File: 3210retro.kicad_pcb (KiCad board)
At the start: 6 copper layers, 44 x 118 mm, 188 parts, among them J801 TEST_2P, P101 USB_OTG, P103 LIPO, P104 DC, P105 EAR, P106 SPEAKER, P107 HEADPHONE, P108 RUMBLE, P301 SEPS525, P801 JTAG, Q501 MMBF170, Q701 MMBF170, SW701 SW_PUSH, SW702 C, SW703 1, SW704 4ghi, SW705 7pqrs, SW706 -, SW707 2abc, SW708 5jkl, SW709 8tuv, SW710 UP, SW711 3def, SW712 6mno, SW713 9wxyz, SW714 *+, SW715 DOWN, SW716 0space, SW717 #up, U1301 LSM9DS1, U201 MAX1555, U202 TPS62742, U203 TPS61021A, U301 TPS61041DBV, U401 LD3985G18R_TSOT23, U402 DRV8601, U403 WM8994ECS/R, U404 MP34DT01TR, U405 MP34DT01TR, U504 A7, U505 SIM_SLOT, U601 ESP-12E, U801 STM32F756VGTx, X101 ANT_GPS, X102 ANT_GSM, Y801 32kHz, Y802 24MHz

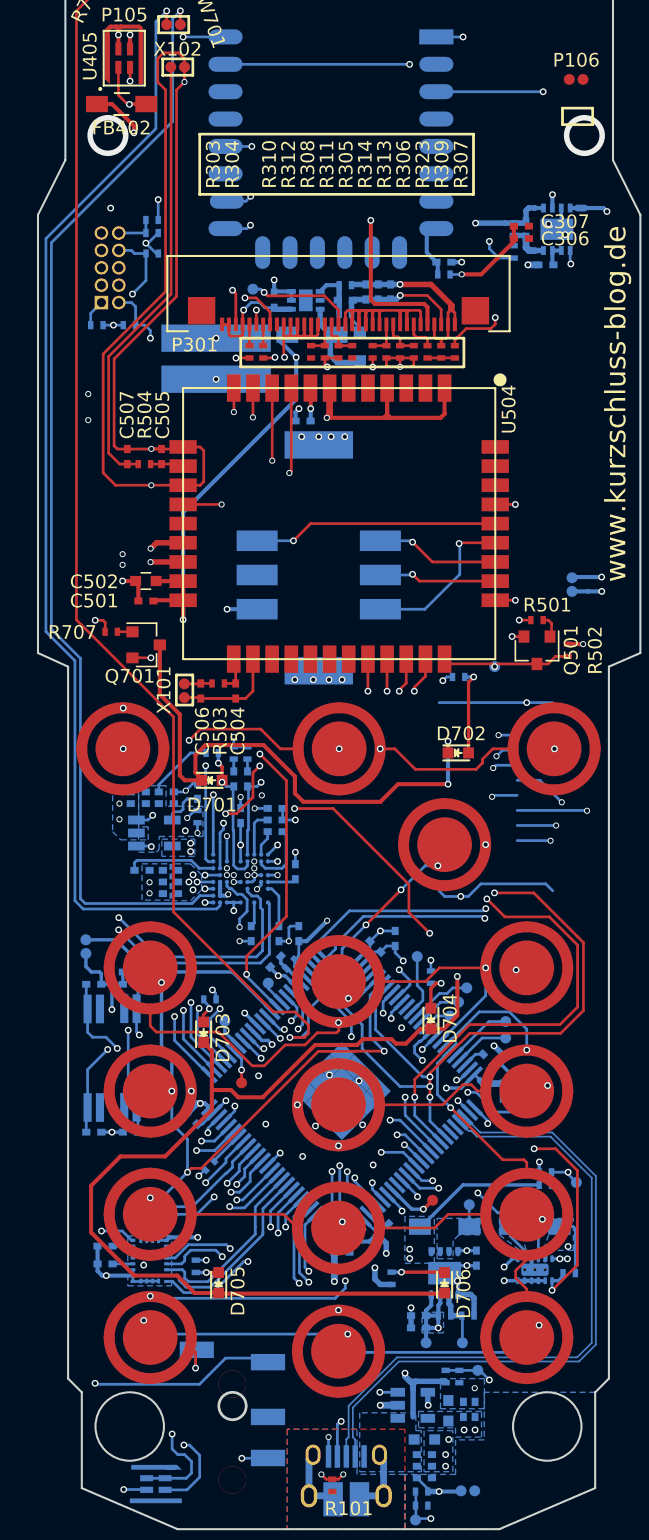
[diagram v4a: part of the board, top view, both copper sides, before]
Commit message: Board Revision 1
* Modified layout of I2C busses
* Added Micro SD footprint back in
* changed layout of crystals
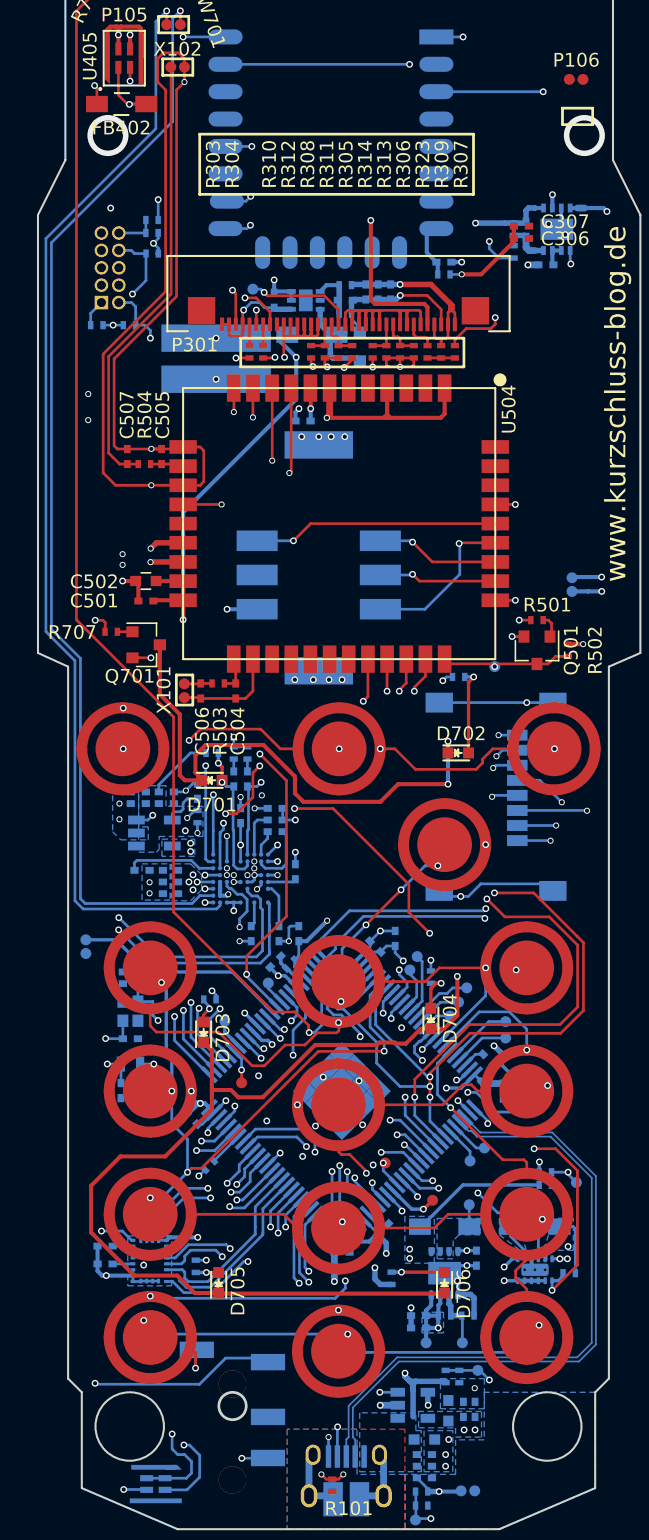
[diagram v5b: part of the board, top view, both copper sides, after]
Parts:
- added J1101: MICRO_SD_HINGE, Connectors:microSD_Card_Receptacle_Wuerth_693072010801, B.Cu at (109.7, 105.6)
- added TP111: TP, NokiaRetroFit:TP, B.Cu at (102.8, 132.3)
- added TP112: TP, NokiaRetroFit:TP, F.Cu at (104.5, 118.2)
- added TP113: TP, NokiaRetroFit:TP, F.Cu at (110.0, 131.2)
- added TP114: TP, NokiaRetroFit:TP, F.Cu at (109.0, 132.2)
- Y801: footprint Crystals:Crystal_SMD_SeikoEpson_MC146-4pin_6.7x1.5mm_HandSoldering -> Crystals:Crystal_SMD_2012-2pin_2.0x1.2mm
- Y802: footprint Crystals:Crystal_SMD_SeikoEpson_MC146-4pin_6.7x1.5mm_HandSoldering -> NokiaRetroFit:Crystal_SMD_ABM11W_4_D1X_T_-4pin_2.0x1.6mm
- moved C804 10.8 mm to (84.1, 119.2)
- moved C802 8.01 mm to (83.5, 127.1), turned to 270 degrees
- moved C801 4.54 mm to (84.8, 127.1), turned to 270 degrees
- moved C803 3.97 mm to (84.1, 123.3), turned to 0 degrees
- moved Y802 3.42 mm to (84.1, 121.3), turned to 90 degrees
- moved Y801 2.72 mm to (84.2, 125.1), turned to 180 degrees
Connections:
- R310 pad 2: /Controller/I2C3_SCL -> /Controller/I2C1_SCL
- R311 pad 2: /Controller/I2C3_SDA -> /Controller/I2C1_SDA
- R801 pad 1: NVCC_3V3 -> 3V3
- R804 pad 1: NVCC_3V3 -> 3V3
- R805 pad 1: NVCC_3V3 -> 3V3
- R807 pad 1: NVCC_3V3 -> 3V3
- U1301 pad 2: /Controller/I2C1_SCL -> /Audio Amplifier/AUDIO_I2C_SCL
- U1301 pad 4: /Controller/I2C1_SDA -> /Audio Amplifier/AUDIO_I2C_SDA
- U403 pad A2: /Audio Amplifier/SPK_OUT- -> Net-(R407-Pad2)
- U403 pad B1: /Audio Amplifier/SPK_OUT+ -> Net-(R406-Pad2)
- U505 pad 5: (no net) -> Net-(U505-Pad5)
- U801 pad 36: Net-(U801-Pad36) -> /Controller/PB2
- U801 pad 55: Net-(U801-Pad55) -> /Controller/PD8
- U801 pad 56: Net-(U801-Pad56) -> /Controller/PD9
- U801 pad 67: Net-(U801-Pad67) -> /Controller/PA8
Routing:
- net NVCC_3V3: track 237.7 -> 149.2 mm, vias 23 -> 20
- net /Audio Amplifier/AUDIO_I2C_SCL: track 43.9 -> 103.7 mm, vias 5 -> 6
- net /Controller/I2C1_SDA: track 12.1 -> 68.4 mm
- net /Controller/I2C1_SCL: track 11.8 -> 67.2 mm, vias 0 -> 2
- net /Audio Amplifier/AUDIO_I2C_SDA: track 33.6 -> 86.7 mm, vias 2 -> 3
- net 3V3: track 188.2 -> 206.1 mm, vias 8 -> 10
- net GND: track 200.2 -> 191.2 mm, vias 81 -> 79
- net Net-(C801-Pad1): track 20.2 -> 12.3 mm
- net Net-(C804-Pad1): track 21.1 -> 15.1 mm
- net /Controller/PB2: track 0.00 -> 3.32 mm
- net /Controller/PD8: track 0.00 -> 2.77 mm
- net /Controller/PD9: track 0.00 -> 2.73 mm
- net Net-(C802-Pad1): track 18.5 -> 15.8 mm
- net /Controller/SYS_WKUP: track 100.0 -> 97.4 mm
- net /Controller/PA8: track 0.00 -> 2.02 mm, vias 0 -> 1
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
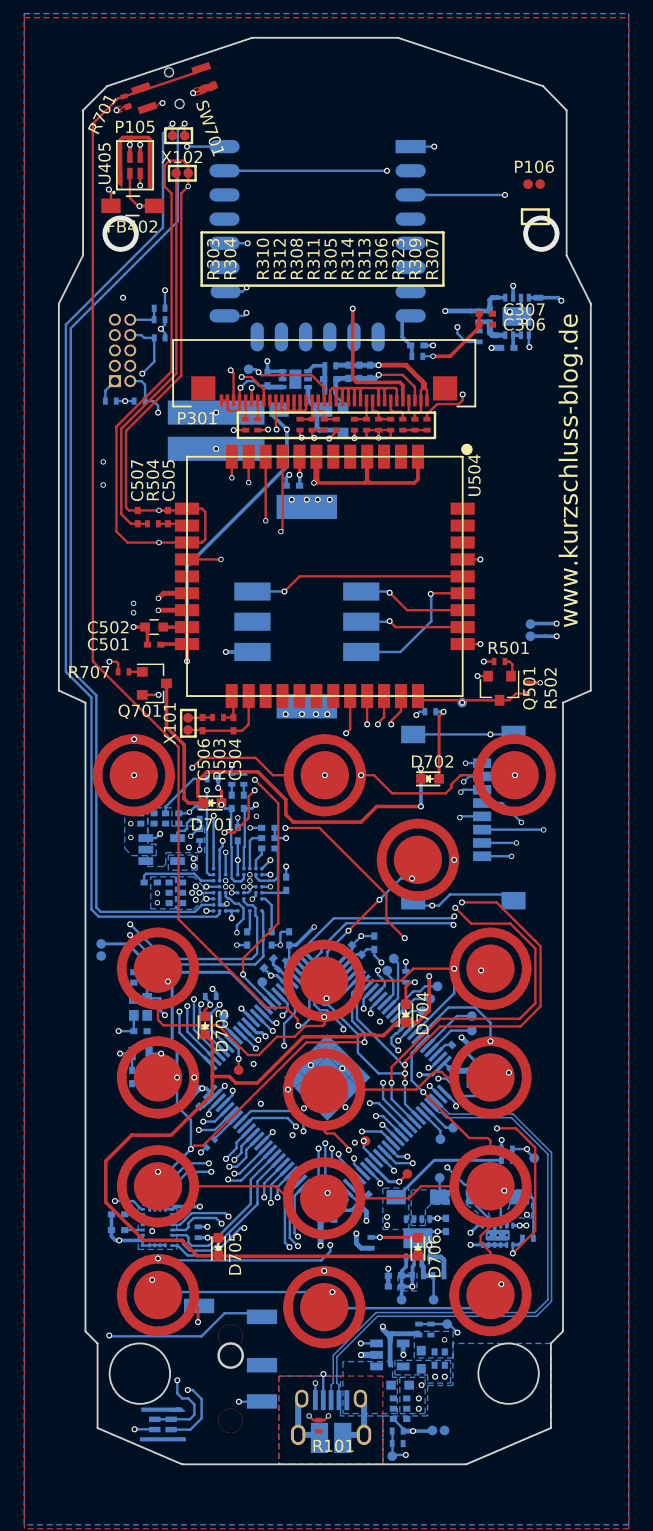
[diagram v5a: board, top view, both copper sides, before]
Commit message: changed sound subsystem
rerouted all the changed tracks
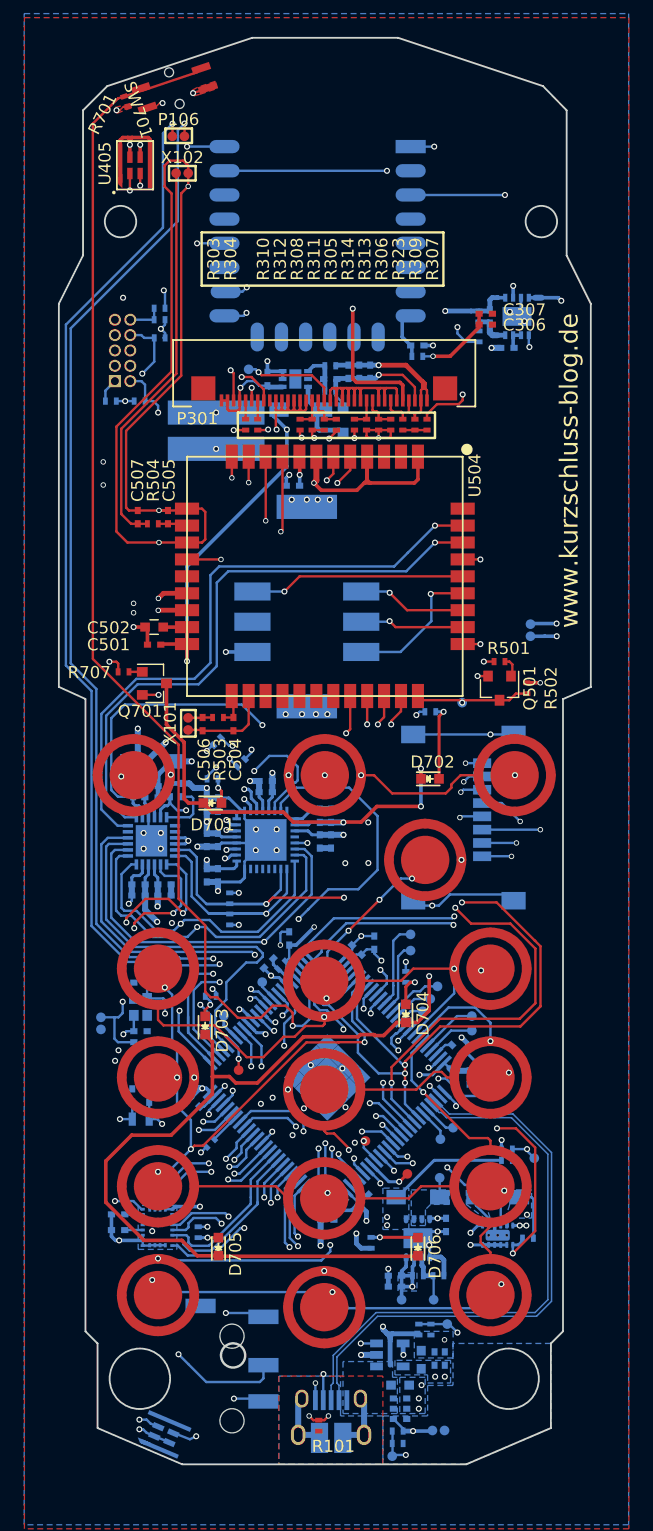
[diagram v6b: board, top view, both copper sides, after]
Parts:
- removed P105: EAR, NokiaRetroFit:SolderWirePad_2x_0,8
- removed R405: 20, Resistors_SMD:R_0402_NoSilk
- added C421: 100n, Capacitors_SMD:C_0402_NoSilk, B.Cu at (90.5, 104.5)
- added C422: 22u, Capacitors_SMD:C_0402_NoSilk, B.Cu at (90.5, 107.5)
- added C423: 100n, Capacitors_SMD:C_0402_NoSilk, B.Cu at (89.6, 107.5)
- added R102: 4k7, Resistors_SMD:R_0402_NoSilk, B.Cu at (91.5, 112.3)
- added R103: 4k7, Resistors_SMD:R_0402_NoSilk, B.Cu at (91.5, 114.0)
- C404: value 4u7 -> 470n
- C405: value 10n -> 470n
- C406: value 1u -> 470n
- C410, C419: value 4u7 -> 100n
- C412, C413: value 1u -> 10u
- C416: value 4u7 -> 10u
- C417: value 100n -> 10u
- C418: value 100n -> 22u
- FB402: moved to B.Cu
- R403: value 10k -> 0
- R404: value 20 -> 0
- U401: value LD3985G18R_TSOT23 -> TLV320ADC3101; footprint TO_SOT_Packages_SMD:TSOT-23-5 -> Housings_DFN_QFN:QFN-24-1EP_4x4mm_Pitch0.5mm
- U403: value WM8994ECS/R -> TLV320DAC3100; footprint NokiaRetroFit:WM8994ECS_SPECIAL -> Housings_DFN_QFN:QFN-32-1EP_5x5mm_Pitch0.5mm
- moved FB402 46.0 mm to (85.0, 101.0)
- moved P106 29.7 mm to (87.3, 49.2)
- moved C411 13.2 mm to (85.0, 103.9), turned to 0 degrees
- moved C419 13.1 mm to (94.5, 102.6), turned to 180 degrees
- moved C416 12.1 mm to (94.5, 103.5), turned to 180 degrees
- moved C410 9.88 mm to (85.0, 103.0)
- moved R403 7.88 mm to (90.5, 99.3), turned to 225 degrees
- moved C413 7.73 mm to (99.9, 107.6), turned to 90 degrees
- moved C420 7.38 mm to (99.0, 105.5)
- moved C403 6.57 mm to (84.0, 112.0), turned to 0 degrees
- moved J801 6.07 mm to (80.9, 122.6)
- moved C417 5.84 mm to (99.9, 105.5), turned to 270 degrees
- moved C405 5.82 mm to (83.5, 103.3)
- moved C805 5.78 mm to (84.1, 124.2), turned to 0 degrees
- moved C414 5.73 mm to (90.5, 110.4), turned to 90 degrees
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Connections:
- net Net-(C801-Pad1) renamed /Controller/RTC_XIN
- net Net-(C802-Pad1) renamed /Controller/RTC_XOUT
- net Net-(C803-Pad1) renamed /Controller/OSC_XIN
- net Net-(C804-Pad1) renamed /Controller/OSC_XOUT
- C401 pad 2: NVCC_3V3 -> NVCC_1V8
- C403 pad 2: NVCC_3V3 -> NVCC_1V8
- C404 pad 1: GND -> /Audio Amplifier/HPM
- C404 pad 2: NVCC_3V3 -> GNDA
- C405 pad 1: Net-(C405-Pad1) -> /Radio Module, GPS and SIM/SPK_+
- C405 pad 2: GND -> GNDA
- C406 pad 1: GND -> /Radio Module, GPS and SIM/SPK_-
- C406 pad 2: NVCC_3V3 -> GNDA
- C408 pad 2: NVCC_1V8 -> +3.3VA
- C409 pad 2: NVCC_1V8 -> +3.3VA
- C410 pad 1: GND -> GNDA
- C410 pad 2: NVCC_1V8 -> +3.3VA
- C411 pad 1: GND -> GNDA
- C411 pad 2: Net-(C411-Pad2) -> +3.3VA
- C412 pad 1: GND -> GNDA
- C412 pad 2: Net-(C412-Pad2) -> +3.3VA
- C413 pad 1: Net-(C413-Pad1) -> GND
- C413 pad 2: GND -> NVCC_1V8
- C414 pad 1: GND -> GNDA
- C414 pad 2: Net-(C414-Pad2) -> +3.3VA
- C415 pad 2: Net-(C415-Pad2) -> NVCC_1V8
- C416 pad 2: Net-(C416-Pad2) -> +3.3VA
- C417 pad 1: Net-(C417-Pad1) -> GND
- C417 pad 2: Net-(C417-Pad2) -> +3.3VA
- C418 pad 1: Net-(C418-Pad1) -> GNDA
- C418 pad 2: /Audio Amplifier/HPL -> 4V_BST
- C419 pad 2: Net-(C419-Pad2) -> +3.3VA
- C420 pad 1: Net-(C420-Pad1) -> GND
- C420 pad 2: /Audio Amplifier/HPR -> +3.3VA
- FB402 pad 2: Net-(FB402-Pad2) -> +3.3VA
- P106 pad 1: Net-(P106-Pad1) -> /Audio Amplifier/SPK_OUT-
- P106 pad 2: Net-(P106-Pad2) -> /Audio Amplifier/SPK_OUT+
- P107 pad 1: GNDA -> Net-(P107-Pad1)
- P107 pad 2: /Audio Amplifier/HPL -> GNDA
- P107 pad 3: Net-(P107-Pad3) -> /Audio Amplifier/HPR
- P107 pad 4: /Audio Amplifier/HPR -> /Audio Amplifier/HPL
- R403 pad 1: Net-(R403-Pad1) -> GND
- R403 pad 2: NVCC_3V3 -> GNDA
- R404 pad 1: Net-(C418-Pad1) -> GND
- R404 pad 2: GND -> GNDA
- U301 pad 1: (no net) -> GND
- U301 pad 2: (no net) -> 4V_BST
- U301 pad 3: (no net) -> 4V_BST
- U301 pad 4: (no net) -> Net-(C304-Pad2)
- U301 pad 6: (no net) -> Net-(D301-Pad2)
- U401 pad 1: NVCC_3V3 -> /Controller/SAI1_SCKA
- U401 pad 2: GND -> /Controller/SAI1_FS
- U401 pad 3: NVCC_3V3 -> /Controller/SAI1_SDA
- U401 pad 4: Net-(C405-Pad1) -> /Audio Amplifier/AUDIO_RESET
- U401 pad 5: NVCC_1V8 -> Net-(U401-Pad5)
- U402 pad 1: (no net) -> /Audio Amplifier/RMBL_EN
- U402 pad 2: (no net) -> Net-(C402-Pad1)
- U402 pad 3: (no net) -> Net-(C402-Pad1)
- U402 pad 4: (no net) -> Net-(C407-Pad2)
- U402 pad 5: (no net) -> /Audio Amplifier/RMBL+
- U402 pad 6: (no net) -> 4V_BST
- U402 pad 7: (no net) -> GND
- U402 pad 8: (no net) -> /Audio Amplifier/RMBL-
- U402 pad 9: (no net) -> GND
- U404 pad 1: Net-(FB402-Pad2) -> +3.3VA
- U404 pad 2: Net-(FB402-Pad2) -> +3.3VA
- U404 pad 3: Net-(U403-PadC6) -> Net-(U401-Pad20)
- U404 pad 4: Net-(U403-PadA9) -> Net-(U401-Pad19)
- U405 pad 1: Net-(FB402-Pad2) -> +3.3VA
- U405 pad 3: Net-(U403-PadC6) -> Net-(U401-Pad20)
- U405 pad 4: Net-(U403-PadA9) -> Net-(U401-Pad19)
- U504 pad 19: /Radio Module, GPS and SIM/MIC_+ -> /Audio Amplifier/AUDIO_IN+
- U504 pad 20: /Radio Module, GPS and SIM/MIC_- -> /Audio Amplifier/AUDIO_IN-
- U801 pad 34: /Controller/AUDIO_INT -> /Audio Amplifier/AUDIO_RESET
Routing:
- net +3.3VA: track 0.00 -> 192.9 mm, vias 0 -> 7
- net Net-(U403-PadC6): track 141.1 -> 0.00 mm, vias 3 -> 0
- net Net-(U403-PadA9): track 134.4 -> 0.00 mm, vias 3 -> 0
- net Net-(U401-Pad20): track 0.00 -> 131.3 mm, vias 0 -> 4
- net Net-(U401-Pad19): track 0.00 -> 129.4 mm, vias 0 -> 4
- net Net-(FB402-Pad2): track 114.9 -> 0.00 mm, vias 2 -> 0
- net /Audio Amplifier/AUDIO_RESET: track 0.00 -> 64.4 mm, vias 0 -> 3
- net /Audio Amplifier/AUDIO_IN-: track 0.00 -> 51.2 mm, vias 0 -> 1
- net /Radio Module, GPS and SIM/SPK_+: track 0.00 -> 50.1 mm, vias 0 -> 2
- net /Audio Amplifier/AUDIO_IN+: track 0.00 -> 49.5 mm, vias 0 -> 1
- net /Radio Module, GPS and SIM/SPK_-: track 0.00 -> 39.7 mm, vias 0 -> 2
- net NVCC_1V8: track 45.0 -> 80.3 mm, vias 9 -> 3
- net GNDA: track 115.3 -> 148.6 mm, vias 3 -> 13
- net /Controller/AUDIO_INT: track 22.7 -> 0.00 mm, vias 2 -> 0
- net /Audio Amplifier/SPK_OUT+: track 80.7 -> 101.3 mm, vias 1 -> 4
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- added copper zone on GND, net GNDA
- removed copper zone on B.Cu, net NVCC_1V8
- removed copper zone on In2.Cu, net NVCC_1V8
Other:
- outline, holes or cut-outs redrawn

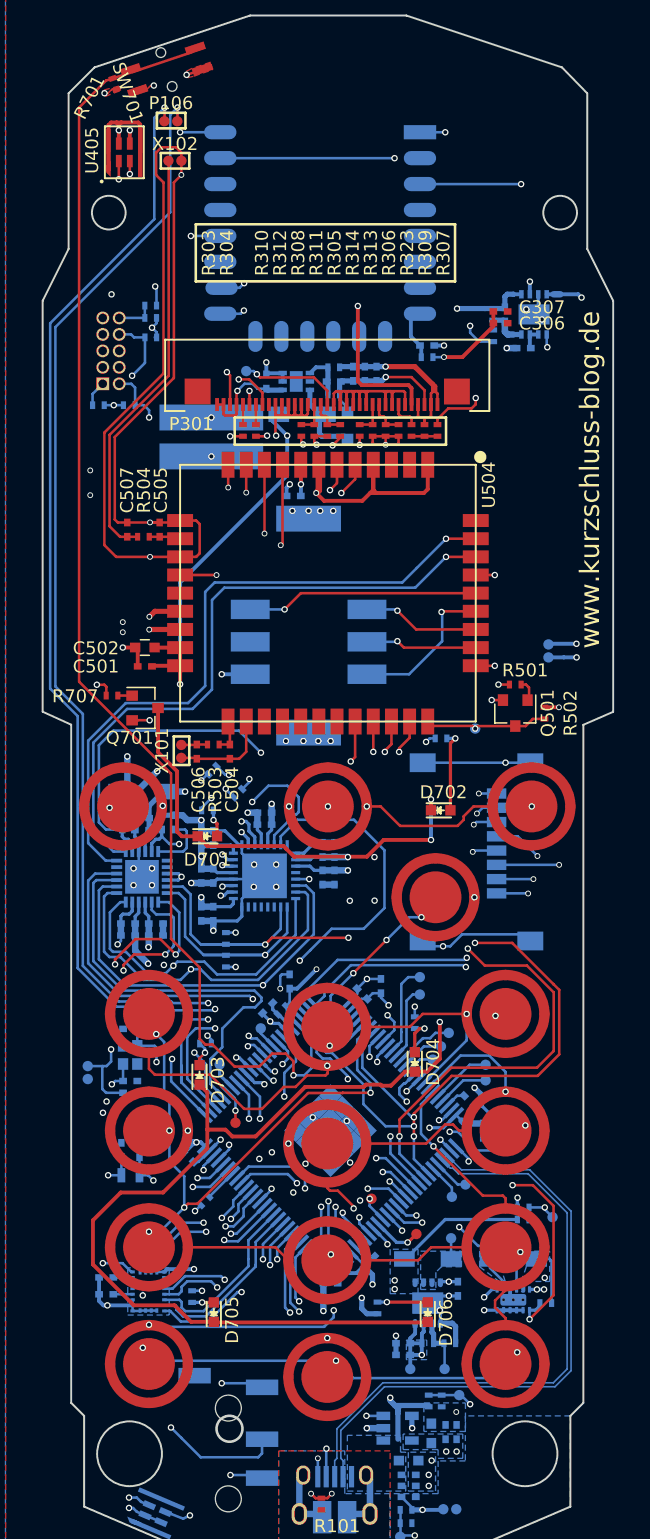
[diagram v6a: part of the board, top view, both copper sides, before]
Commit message: worked on DRC messages
* shuffeling tracks around to avoid vias
* shuffeling vias around to avoid tracks
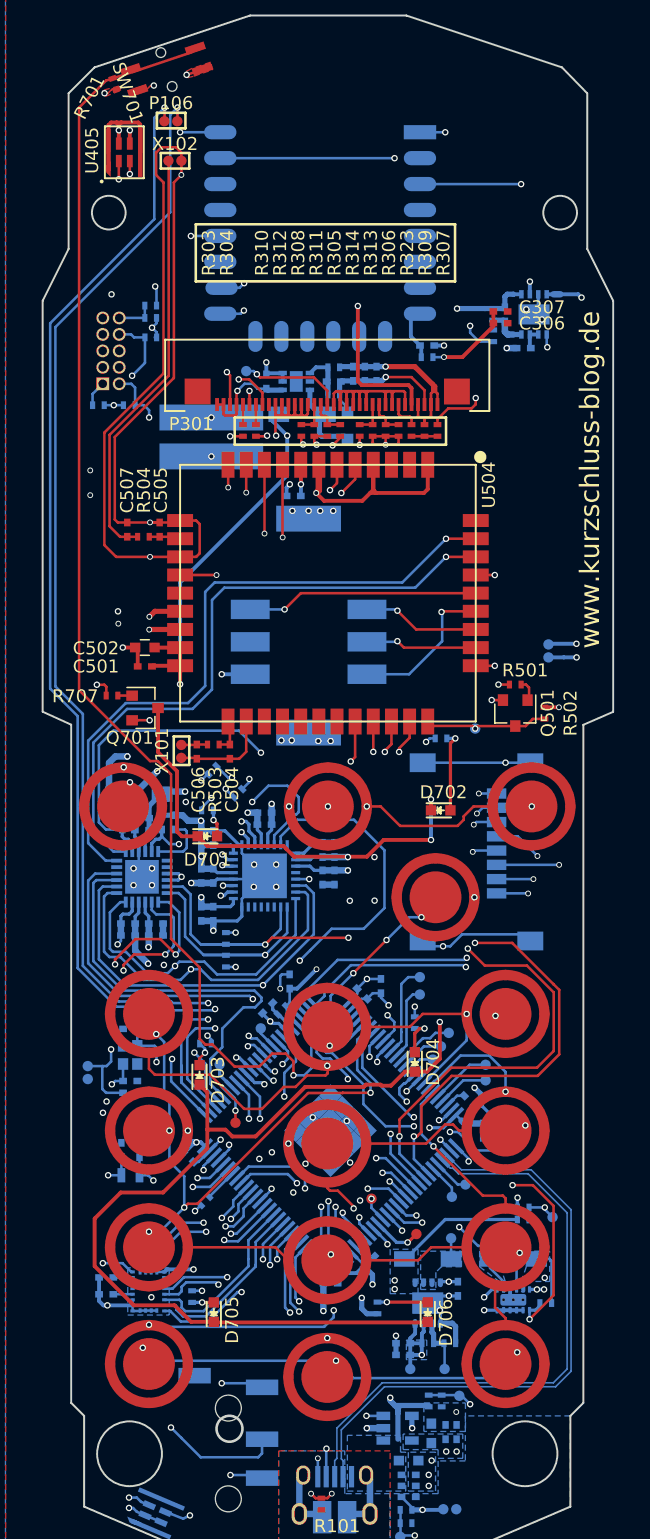
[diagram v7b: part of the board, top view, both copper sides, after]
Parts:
- moved FB402 0.32 mm to (84.8, 101.2)
- moved TP201 0.05 mm to (109.5, 147.6)
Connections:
- U401 pad 25: (no net) -> GNDA
- U403 pad 33: (no net) -> GNDA
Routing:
- net /Buttons and LEDs/KEYPAD_ROW3: track 148.4 -> 152.7 mm, vias 6 -> 7
- net +3.3VA: track 192.9 -> 194.8 mm
- net /Radio Module, GPS and SIM/AT_UART_TX: track 67.5 -> 69.2 mm
- net NVCC_3V3: track 151.8 -> 153.0 mm
- net /Buttons and LEDs/KEYPAD_COL0: track 84.5 -> 85.5 mm
- net Net-(U401-Pad20): track 131.3 -> 132.1 mm
- net /Radio Module, GPS and SIM/AT_UART_RX: track 66.5 -> 65.8 mm
- net GNDA: track 148.6 -> 148.7 mm, vias 13 -> 16
- net (no net): vias 4 -> 1
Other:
- net class Default: clearance 0.2 -> 0.199
- rule trace_clearance: 0.2 -> 0.199
